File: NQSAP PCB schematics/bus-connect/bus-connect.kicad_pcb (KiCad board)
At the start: 2 copper layers, 102 x 22 mm, 18 parts, among them J1 Bus, J2 Bus

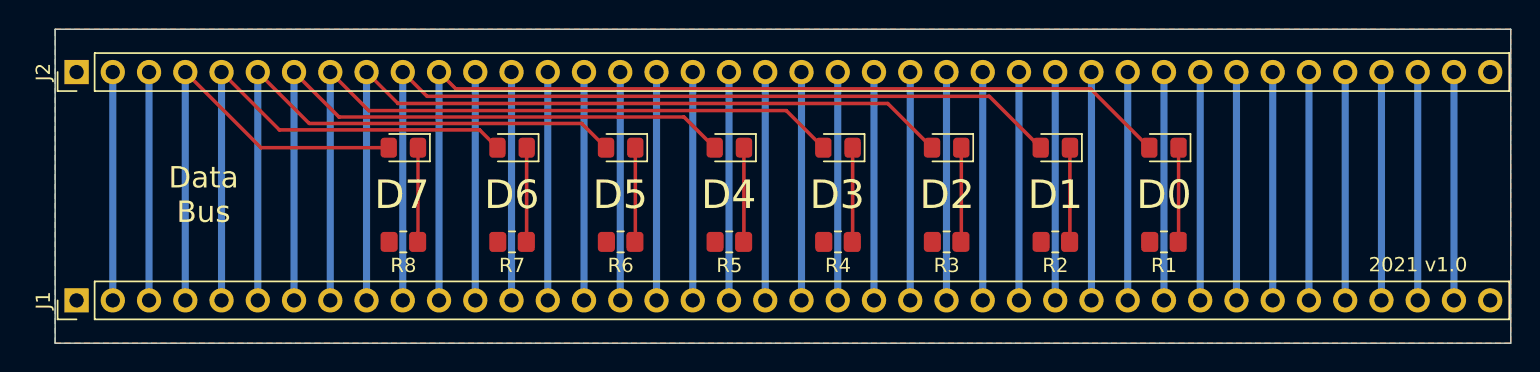
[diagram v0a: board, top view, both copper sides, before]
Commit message: Add RAM, update and add gerbers for new boards
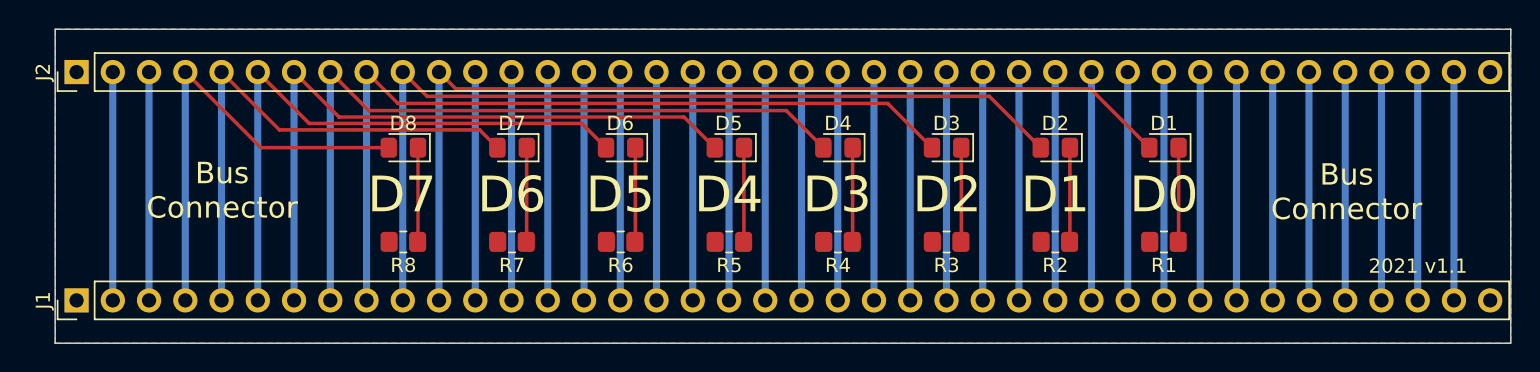
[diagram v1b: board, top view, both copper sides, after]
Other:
- board text added: "2021 v1.1"
- board text removed: "2021 v1.0"
- board text removed: "Data Bus"
